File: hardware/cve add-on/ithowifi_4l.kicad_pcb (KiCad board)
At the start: 4 copper layers, 42.3 x 51.5 mm, 32 parts, among them J1 CONN_01X07, J2 conn, J3 Conn_Coaxial, J4 TC2030-MCP-NL, J5 Conn_02x02_Odd_Even, Q1 BSS138, Q2 BSS138, SW1 Fail safe, SW2 Reset, U1 ESP32-WROOM, U2 CC1101-868MHz-Module

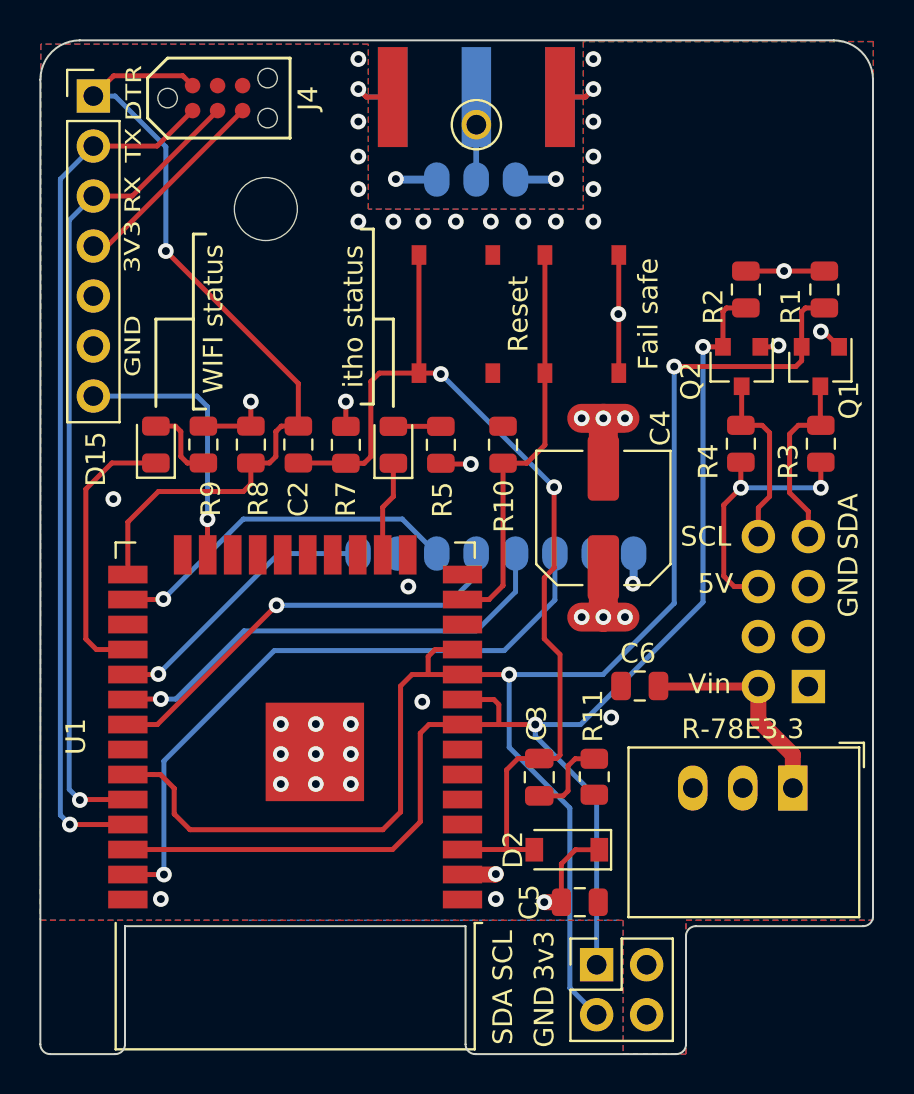
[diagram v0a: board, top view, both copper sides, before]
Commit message: Version 2.3-beta5
- fix: prevent crashes unsupported or partly supported itho devices
- breaking: On the up-side; all settings and labels have been regenerated and checked (and some translated) with a script, units have been added where available and labels are more descriptive. On the flip-side; automations based on the API, specifically the itho status label based automations might need to be updated.
- add: support for itho HeatPumt (WPU) devices and AutoTemp devices.

Please check labels for status and settings, if you see anything wrong, please let me know.
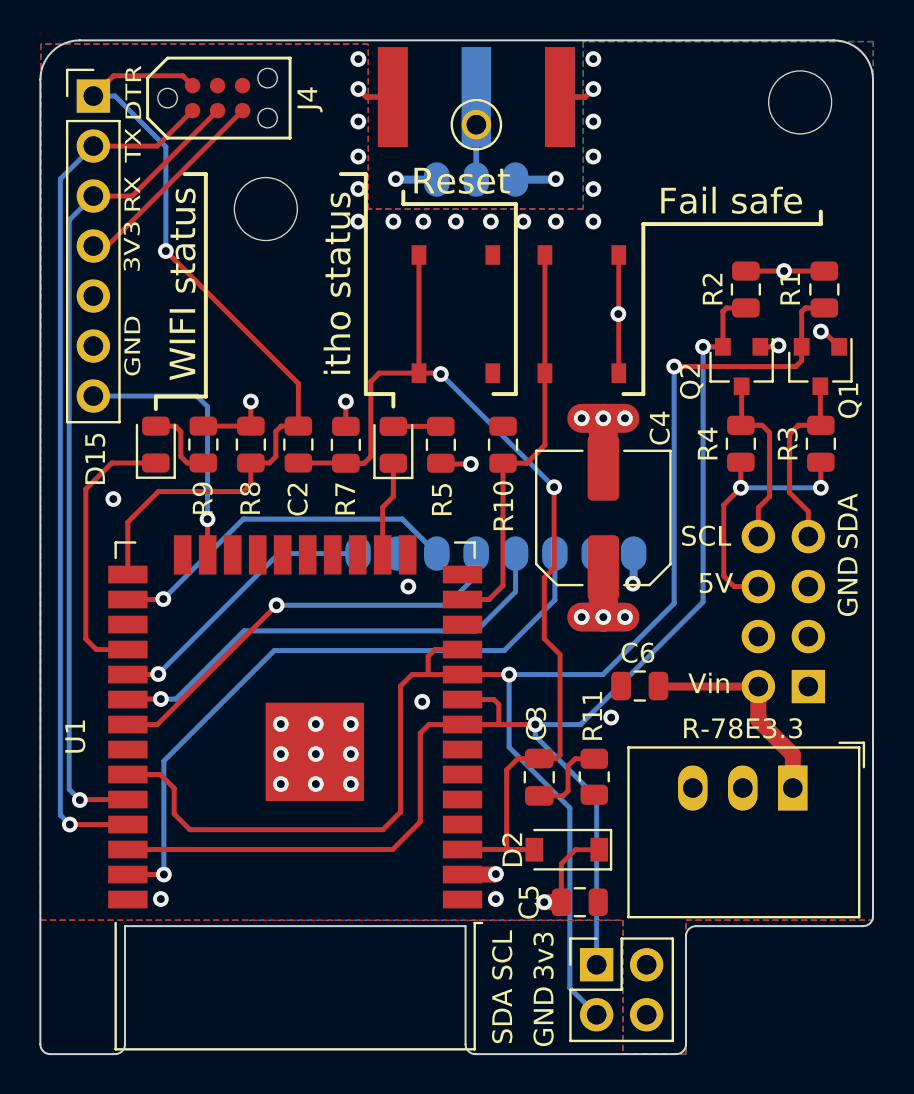
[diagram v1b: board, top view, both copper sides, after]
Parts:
- added H3: MountingHole, MountingHole:MountingHole_2.5mm, F.Cu at (121.6, 108.1)
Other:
- board text added: "Itho CVE ESP WiFi Controller v2.10 Arjen Hiemstra - GNU GPL 3.0"
- board text removed: "Itho CVE ESP WiFi Controller v2.9 Arjen Hiemstra - GNU GPL 3.0"

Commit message: Update HW files and correct spelling
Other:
- board text added: "Itho CVE ESP WiFi Controller v2.11 Arjen Hiemstra - GNU GPL 3.0"
- board text added: "NL5"
- board text removed: "Itho CVE ESP WiFi Controller v2.10 Arjen Hiemstra - GNU GPL 3.0"

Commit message: Update hardware design files
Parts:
- U1: footprint RF_Module:ESP32-WROOM-32 -> nrg_watch:ESP32-WROOM-32E
- moved U1 1.24 mm to (96.0, 141.6)
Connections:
- net D0/RX0 renamed D0/RX0
- net D1/TX0 renamed D1/TX0
- J1 pad 5: Net-(J1-Pad5) -> unconnected-(J1-Pad5)
- J2 pad 1: Net-(J2-Pad1) -> unconnected-(J2-Pad1)
- J2 pad 3: Net-(J2-Pad3) -> unconnected-(J2-Pad3)
- J2 pad 4: Net-(J2-Pad4) -> unconnected-(J2-Pad4)
- J4 pad 6: Net-(J4-Pad6) -> unconnected-(J4-Pad6)
- U1 pad 12: Net-(U1-Pad12) -> unconnected-(U1-Pad12)
- U1 pad 14: Net-(U1-Pad14) -> unconnected-(U1-Pad14)
- U1 pad 17: Net-(U1-Pad17) -> unconnected-(U1-Pad17)
- U1 pad 18: Net-(U1-Pad18) -> unconnected-(U1-Pad18)
- U1 pad 19: Net-(U1-Pad19) -> unconnected-(U1-Pad19)
- U1 pad 20: Net-(U1-Pad20) -> unconnected-(U1-Pad20)
- U1 pad 21: Net-(U1-Pad21) -> unconnected-(U1-Pad21)
- U1 pad 22: Net-(U1-Pad22) -> unconnected-(U1-Pad22)
- U1 pad 24: Net-(U1-Pad24) -> unconnected-(U1-Pad24)
- U1 pad 27: Net-(U1-Pad27) -> unconnected-(U1-Pad27)
- U1 pad 32: Net-(U1-Pad32) -> unconnected-(U1-Pad32)
- U1 pad 4: Net-(U1-Pad4) -> unconnected-(U1-Pad4)
- U1 pad 5: Net-(U1-Pad5) -> unconnected-(U1-Pad5)
- U1 pad 6: Net-(U1-Pad6) -> unconnected-(U1-Pad6)
- U1 pad 7: Net-(U1-Pad7) -> unconnected-(U1-Pad7)
- U2 pad 7: Net-(U2-Pad7) -> unconnected-(U2-Pad7)
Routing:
- net D4_IRQ: track 18.1 -> 19.0 mm
- net SDA_L: track 82.5 -> 83.0 mm
- net D18_SCK: track 23.9 -> 24.4 mm
- added copper zone on In1.Cu, net +3V3
- added copper zone on In2.Cu, net GND
- removed copper zone on 3V3, net +3V3
- removed copper zone on GND, net GND
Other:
- net class Default removed
- board text added: "HW rev.: 2 Batch: 13-0622"
- board text added: "Itho CVE WiFi Controller Arjen Hiemstra - GNU GPL 3.0"
- board text removed: "Itho CVE ESP WiFi Controller v2.11 Arjen Hiemstra - GNU GPL 3.0"

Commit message: update hardware files
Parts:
- Q1, Q2: footprint Package_TO_SOT_SMD:SOT-23 -> Package_TO_SOT_SMD:SOT-23W
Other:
- board text added: "HW rev.: 2 Batch: 14-1222"
- board text added: "Itho CVE WiFi Controller Arjen Hiemstra - GNU GPL 3.0 https://github.com/arjenhiemstra/ithowifi"
- board text removed: "HW rev.: 2 Batch: 13-0622"
- board text removed: "Itho CVE WiFi Controller Arjen Hiemstra - GNU GPL 3.0"
- board text removed: "https://github.com/arjenhiemstra/ithowifi"

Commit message: Update hardware files
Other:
- board text added: "HW rev.: 2 Batch: 15-1722"
- board text removed: "HW rev.: 2 Batch: 14-1222"
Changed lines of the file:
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@@
       (drillshape 0)
       (scaleselection 1)
-      (outputdirectory "gerbers 2.14 4layer/")
+      (outputdirectory "gerbers 2.15 4layer/")
     )
   )
@@
     (fp_circle (center 0 0) (end 2.5 0) (layer "Cmts.User") (width 0.15) (fill none))
     (fp_circle (center 0 0) (end 2.75 0) (layer "F.CrtYd") (width 0.05) (fill none))
-    (pad "" np_thru_hole circle (at 0 0) (size 2.5 2.5) (drill 2.5) (layers *.Cu *.Mask))
+    (pad "" np_thru_hole circle (at 0 0) (size 3.5 3.5) (drill 3.2) (layers F&B.Cu *.Mask))
   )
   (footprint "LED_SMD:LED_0805_2012Metric" (layer "F.Cu")
@@
     (fp_circle (center 0 0) (end 2.5 0) (layer "Cmts.User") (width 0.15) (fill none))
     (fp_circle (center 0 0) (end 2.75 0) (layer "F.CrtYd") (width 0.05) (fill none))
-    (pad "" np_thru_hole circle (at 0 0) (size 2.5 2.5) (drill 2.5) (layers *.Cu *.Mask))
+    (pad "" np_thru_hole circle (at 0 0) (size 3.5 3.5) (drill 3.2) (layers F&B.Cu *.Mask))
   )
   (footprint "Connector_PinSocket_2.54mm:PinSocket_2x04_P2.54mm_Vertical" (layer "B.Cu")
@@
     (effects (font (size 1.246 1.246) (thickness 0.2)) (justify right mirror))
   )
-  (gr_text "HW rev.: 2\nBatch: 14-1222" (at 103.378 148.971 90) (layer "B.SilkS")
+  (gr_text "HW rev.: 2\nBatch: 15-1722" (at 103.378 148.971 90) (layer "B.SilkS")
     (effects (font (size 1.246 1.246) (thickness 0.2)) (justify right mirror))
   )

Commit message: Update hardware files
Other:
- board text added: "HW rev.: 2 Batch: 18-3422"
- board text removed: "HW rev.: 2 Batch: 15-1722"
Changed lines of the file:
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@@
       (drillshape 0)
       (scaleselection 1)
-      (outputdirectory "gerbers 2.15 4layer/")
+      (outputdirectory "gerbers 2.18 4layer/")
     )
   )
@@
     (fp_circle (center 0 0) (end 2.5 0) (layer "Cmts.User") (width 0.15) (fill none))
     (fp_circle (center 0 0) (end 2.75 0) (layer "F.CrtYd") (width 0.05) (fill none))
-    (pad "" np_thru_hole circle (at 0 0) (size 3.5 3.5) (drill 3.2) (layers F&B.Cu *.Mask))
+    (pad "" np_thru_hole circle (at 0 0) (size 3.2 3.2) (drill 3.2) (layers F&B.Cu *.Mask))
   )
   (footprint "LED_SMD:LED_0805_2012Metric" (layer "F.Cu")
@@
     (fp_circle (center 0 0) (end 2.5 0) (layer "Cmts.User") (width 0.15) (fill none))
     (fp_circle (center 0 0) (end 2.75 0) (layer "F.CrtYd") (width 0.05) (fill none))
-    (pad "" np_thru_hole circle (at 0 0) (size 3.5 3.5) (drill 3.2) (layers F&B.Cu *.Mask))
+    (pad "" np_thru_hole circle (at 0 0) (size 3.2 3.2) (drill 3.2) (layers F&B.Cu *.Mask))
   )
   (footprint "Connector_PinSocket_2.54mm:PinSocket_2x04_P2.54mm_Vertical" (layer "B.Cu")
@@
     (effects (font (size 1.246 1.246) (thickness 0.2)) (justify right mirror))
   )
-  (gr_text "HW rev.: 2\nBatch: 15-1722" (at 103.378 148.971 90) (layer "B.SilkS")
+  (gr_text "HW rev.: 2\nBatch: 18-3422" (at 103.378 148.971 90) (layer "B.SilkS")
     (effects (font (size 1.246 1.246) (thickness 0.2)) (justify right mirror))
   )
